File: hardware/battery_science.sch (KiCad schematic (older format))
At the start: 1 part

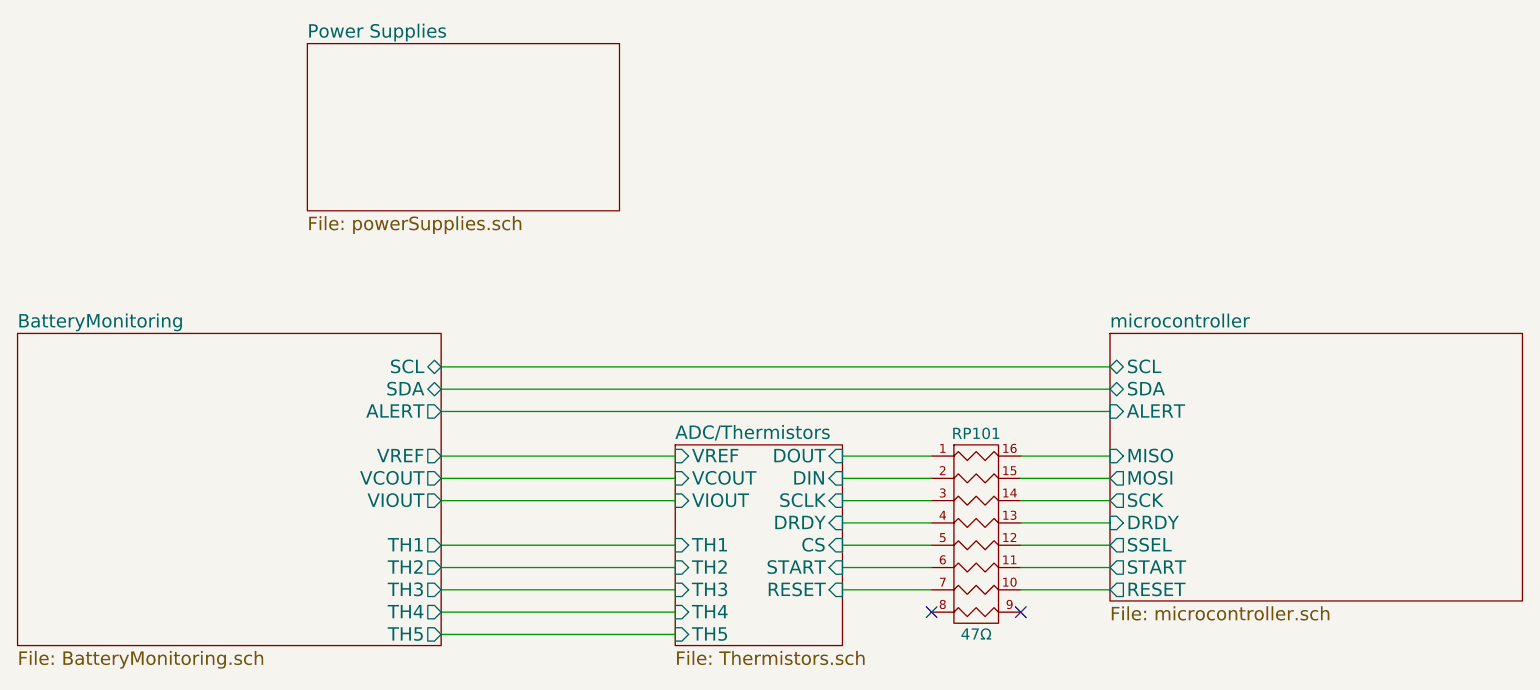
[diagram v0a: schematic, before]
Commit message: Updated pcb layout
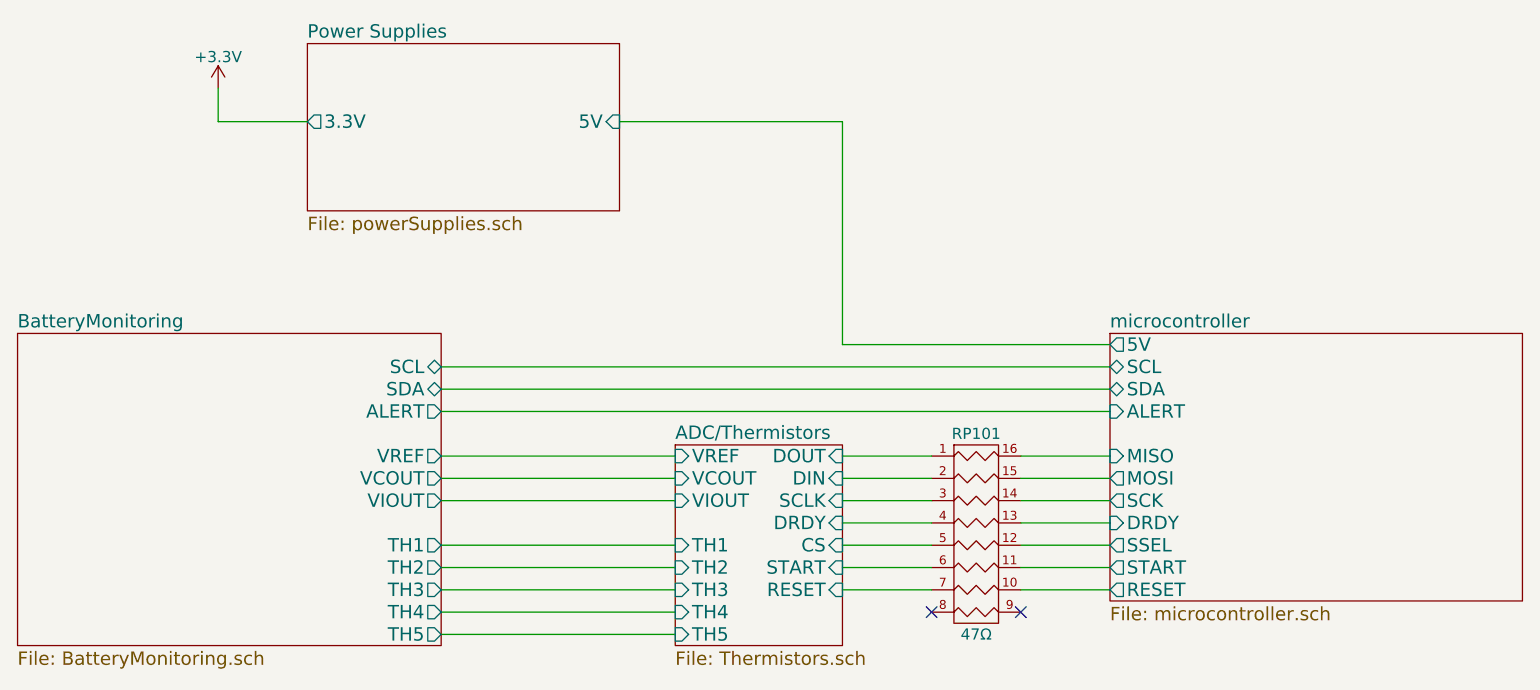
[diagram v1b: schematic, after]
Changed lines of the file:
@@
 F10 "START" O L 7200 3600 60
 F11 "RESET" O L 7200 3700 60
+F12 "5V" O L 7200 2600 60
 $EndSheet
 $Sheet
@@
 F0 "Power Supplies" 60
 F1 "powerSupplies.sch" 60
+F2 "3.3V" O L 3600 1600 60
+F3 "5V" I R 5000 1600 60
 $EndSheet
 Wire Wire Line
@@
 Wire Wire Line
 	6800 3700 7200 3700
+Wire Wire Line
+	7200 2600 6000 2600
+Wire Wire Line
+	6000 2600 6000 1600
+Wire Wire Line
+	6000 1600 5000 1600
+$Comp
+L +3.3V #PWR01
+U 1 1 57F01614
+P 3200 1450
+F 0 "#PWR01" H 3200 1300 50  0001 C CNN
+F 1 "+3.3V" H 3200 1590 50  0000 C CNN
+F 2 "" H 3200 1450 60  0000 C CNN
+F 3 "" H 3200 1450 60  0000 C CNN
+	1    3200 1450
+	1    0    0    -1
+$EndComp
+Wire Wire Line
+	3600 1600 3200 1600
+Wire Wire Line
+	3200 1600 3200 1450
 $EndSCHEMATC
